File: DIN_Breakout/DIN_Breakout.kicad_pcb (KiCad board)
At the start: 2 copper layers, 33 x 23.2 mm, 2 parts, among them J1 Matra Alice, J2 Conn_01x08

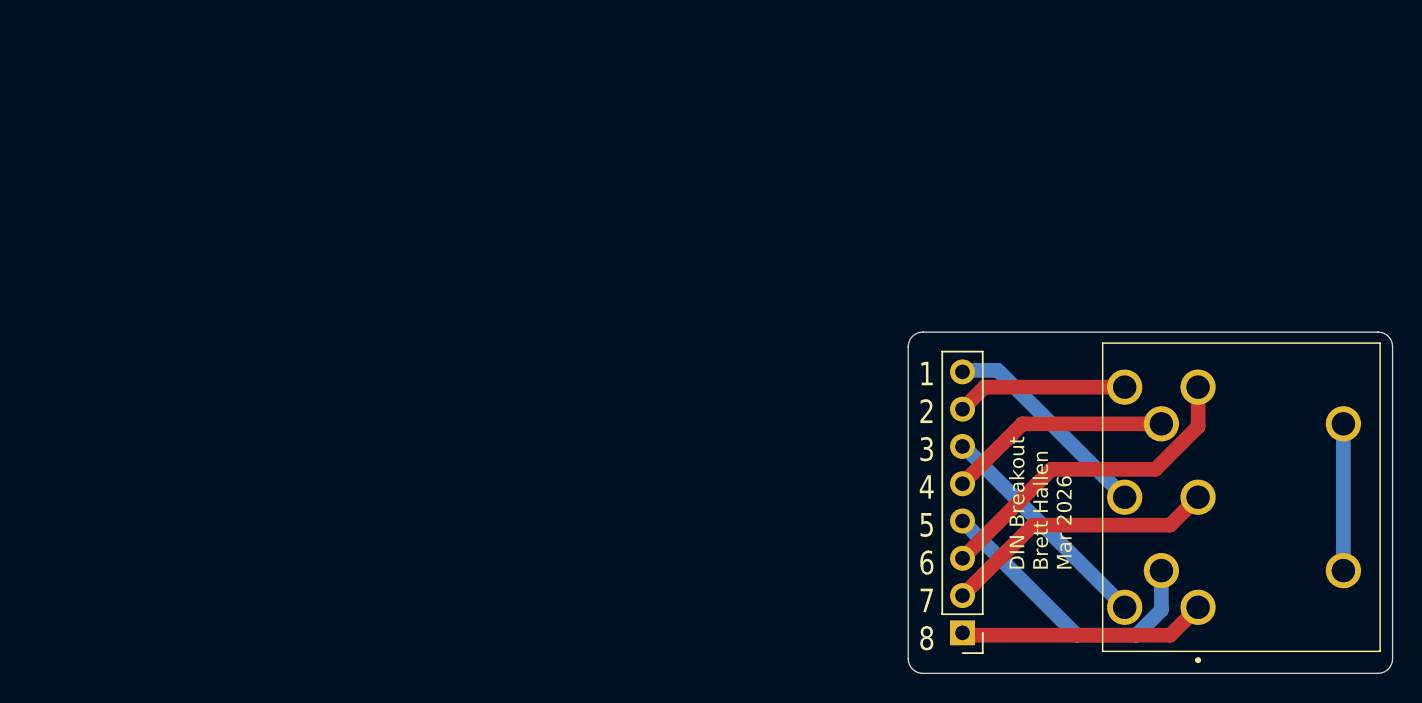
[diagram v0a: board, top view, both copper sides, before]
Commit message: Corrected silkscreen pin numbering
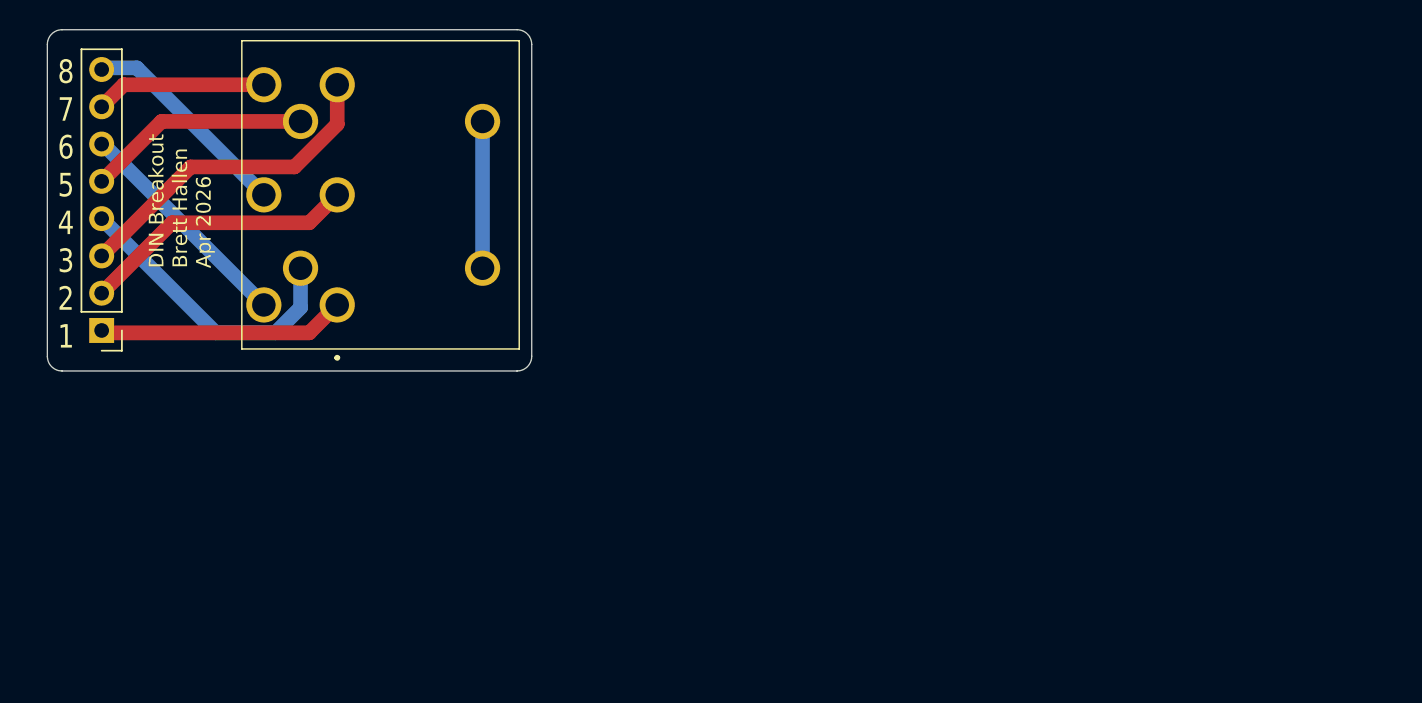
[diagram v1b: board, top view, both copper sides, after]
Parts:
- moved J1 62.2 mm to (93.4, 68.4)
- moved J2 62.2 mm to (77.3, 70.1)
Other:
- board text added: "DIN Breakout Brett Hallen Apr 2026"
- board text removed: "1 2 3 4 5 6 7 8"
- board text removed: "DIN Breakout Brett Hallen Mar 2026"
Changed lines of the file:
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@@
 		(legacy_teardrops no)
 	)
-	(paper "A4")
+	(paper "A5")
 	(title_block
 		(title "5/6/7/8 pin DIN Breakout Board")
-		(date "9/MAR/2026")
+		(date "29/APR/2026")
 		(rev "A")
 		(company "Brett Hallen")
@@
 	(footprint "Connector_PinHeader_2.54mm:PinHeader_1x08_P2.54mm_Vertical"
 		(layer "F.Cu")
-		(at 135.95 90.74 180)
+		(at 77.301 70.139 180)
 		(descr "Through hole straight pin header, 1x08, 2.54mm pitch, single row")
 		(tags "Through hole pin header THT 1x08 2.54mm single row")
@@
 	(footprint "Clueless_Engineer:6710801"
 		(layer "F.Cu")
-		(at 152 89 -90)
+		(at 93.351 68.399 -90)
 		(descr "DIN8")
 		(tags "Connector, DIN8")
@@
 	)
 	(gr_arc
-		(start 132.25 71.25)
-		(mid 132.542893 70.542893)
-		(end 133.25 70.25)
+		(start 73.601 50.649)
+		(mid 73.893893 49.941893)
+		(end 74.601 49.649)
 		(stroke
 			(width 0.05)
@@
 	)
 	(gr_line
-		(start 133.25 70.25)
-		(end 164.25 70.25)
+		(start 74.601 49.649)
+		(end 105.601 49.649)
 		(stroke
 			(width 0.05)
@@
 	)
 	(gr_arc
-		(start 164.25 70.25)
-		(mid 164.957107 70.542893)
-		(end 165.25 71.25)
+		(start 105.601 49.649)
+		(mid 106.308107 49.941893)
+		(end 106.601 50.649)
 		(stroke
 			(width 0.05)
@@
 	)
 	(gr_line
-		(start 165.25 71.25)
-		(end 165.25 92.5)
+		(start 106.601 50.649)
+		(end 106.601 71.899)
 		(stroke
 			(width 0.05)
@@
 	)
 	(gr_arc
-		(start 133.25 93.5)
-		(mid 132.542893 93.207107)
-		(end 132.25 92.5)
+		(start 74.601 72.899)
+		(mid 73.893893 72.606107)
+		(end 73.601 71.899)
 		(stroke
 			(width 0.05)
@@
 	)
 	(gr_line
-		(start 164.25 93.5)
-		(end 133.25 93.5)
+		(start 105.601 72.899)
+		(end 74.601 72.899)
 		(stroke
 			(width 0.05)
@@
 	)
 	(gr_line
-		(start 132.25 92.5)
-		(end 132.25 71.25)
+		(start 73.601 71.899)
+		(end 73.601 50.649)
 		(stroke
 			(width 0.05)
@@
 	)
 	(gr_arc
-		(start 165.25 92.5)
-		(mid 164.957107 93.207107)
-		(end 164.25 93.5)
+		(start 106.601 71.899)
+		(mid 106.308107 72.606107)
+		(end 105.601 72.899)
 		(stroke
 			(width 0.05)
@@
 		(layer "Edge.Cuts")
 	)
-	(gr_text "1\n2\n3\n4\n5\n6\n7\n8"
-		(at 132.95 92.1 0)
+	(gr_text "8\n7\n6\n5\n4\n3\n2\n1"
+		(at 74.301 71.499 0)
 		(layer "F.SilkS")
 		(effects
@@
 		)
 	)
-	(gr_text "DIN Breakout\nBrett Hallen\nMar 2026"
-		(at 143.5 86.5 90)
+	(gr_text "DIN Breakout\nBrett Hallen\nApr 2026"
+		(at 84.851 65.899 90)
 		(layer "F.SilkS")
 		(effects
@@
 	)
 	(gr_text "2"
-		(at 154.95 82.6 0)
+		(at 96.301 61.999 0)
 		(layer "B.SilkS")
 		(effects
@@
 	)
 	(gr_text "7"
-		(at 149.7 75.1 0)
+		(at 91.051 54.499 0)
 		(layer "B.SilkS")
 		(effects
@@
 	)
 	(gr_text "8\n7\n6\n5\n4\n3\n2\n1"
-		(at 134.45 92.1 0)
+		(at 75.801 71.499 0)
 		(layer "B.SilkS")
 		(effects
@@
 	)
 	(gr_text "3"
-		(at 154.95 75.1 0)
+		(at 96.301 54.499 0)
 		(layer "B.SilkS")
 		(effects
@@
 	)
 	(gr_text "4"
-		(at 152.45 87.5 0)
+		(at 93.801 66.899 0)
 		(layer "B.SilkS")
 		(effects
@@
 	)
 	(gr_text "6"
-		(at 149.7 90.1 0)
+		(at 91.051 69.499 0)
 		(layer "B.SilkS")
 		(effects
@@
 	)
 	(gr_text "1"
-		(at 154.7 90.1 0)
+		(at 96.051 69.499 0)
 		(layer "B.SilkS")
 		(effects
@@
 	)
 	(gr_text "5"
-		(at 152.7 77.6 0)
+		(at 94.051 56.999 0)
 		(layer "B.SilkS")
 		(effects
@@
 	)
 	(gr_text "8"
-		(at 149.7 82.6 0)
+		(at 91.051 61.999 0)
 		(layer "B.SilkS")
 		(effects
@@
 	)
 	(segment
-		(start 138.35 72.85)
-		(end 136.06 72.85)
+		(start 79.701 52.249)
+		(end 77.411 52.249)
 		(width 1)
 		(layer "B.Cu")
@@
 	)
 	(segment
-		(start 136.06 72.85)
-		(end 135.95 72.96)
+		(start 77.411 52.249)
+		(end 77.301 52.359)
 		(width 1)
 		(layer "B.Cu")
@@
 	)
 	(segment
-		(start 147 81.5)
-		(end 138.35 72.85)
+		(start 88.351 60.899)
+		(end 79.701 52.249)
 		(width 1)
 		(layer "B.Cu")
@@
 	)
 	(segment
-		(start 140.749 83.401)
-		(end 135.95 88.2)
+		(start 82.1 62.8)
+		(end 77.301 67.599)
 		(width 1)
 		(layer "F.Cu")
@@
 	)
 	(segment
-		(start 150.099 83.401)
-		(end 140.749 83.401)
+		(start 91.45 62.8)
+		(end 82.1 62.8)
 		(width 1)
 		(layer "F.Cu")
@@
 	)
 	(segment
-		(start 152 81.5)
-		(end 150.099 83.401)
+		(start 93.351 60.899)
+		(end 91.45 62.8)
 		(width 1)
 		(layer "F.Cu")
@@
 	)
 	(segment
-		(start 161.9 76.5)
-		(end 161.9 86.5)
+		(start 103.251 55.899)
+		(end 103.251 65.899)
 		(width 1)
 		(layer "B.Cu")
@@
 	)
 	(segment
-		(start 147 89)
-		(end 136.04 78.04)
+		(start 88.351 68.399)
+		(end 77.391 57.439)
 		(width 1)
 		(layer "B.Cu")
@@
 	)
 	(segment
-		(start 136.04 78.04)
-		(end 135.95 78.04)
+		(start 77.391 57.439)
+		(end 77.301 57.439)
 		(width 1)
 		(layer "B.Cu")
@@
 	)
 	(segment
-		(start 149.5 76.5)
-		(end 140.03 76.5)
+		(start 90.851 55.899)
+		(end 81.381 55.899)
 		(width 1)
 		(layer "F.Cu")
@@
 	)
 	(segment
-		(start 140.03 76.5)
-		(end 135.95 80.58)
+		(start 81.381 55.899)
+		(end 77.301 59.979)
 		(width 1)
 		(layer "F.Cu")
@@
 	)
 	(segment
-		(start 137.45 74)
-		(end 135.95 75.5)
+		(start 78.801 53.399)
+		(end 77.301 54.899)
 		(width 1)
 		(layer "F.Cu")
@@
 	)
 	(segment
-		(start 147 74)
-		(end 137.45 74)
+		(start 88.351 53.399)
+		(end 78.801 53.399)
 		(width 1)
 		(layer "F.Cu")
@@
 	)
 	(segment
-		(start 143.731 90.901)
-		(end 135.95 83.12)
+		(start 85.082 70.3)
+		(end 77.301 62.519)
 		(width 1)
 		(layer "B.Cu")
@@
 	)
 	(segment
-		(start 149.5 86.5)
-		(end 149.5 89.18842)
+		(start 90.851 65.899)
+		(end 90.851 68.58742)
 		(width 1)
 		(layer "B.Cu")
@@
 	)
 	(segment
-		(start 147.78742 90.901)
-		(end 143.731 90.901)
+		(start 89.13842 70.3)
+		(end 85.082 70.3)
 		(width 1)
 		(layer "B.Cu")
@@
 	)
 	(segment
-		(start 149.5 89.18842)
-		(end 147.78742 90.901)
+		(start 90.851 68.58742)
+		(end 89.13842 70.3)
 		(width 1)
 		(layer "B.Cu")
@@
 	)
 	(segment
-		(start 142.011 79.599)
-		(end 135.95 85.66)
+		(start 83.362 58.998)
+		(end 77.301 65.059)
 		(width 1)
 		(layer "F.Cu")
@@
 	)
 	(segment
-		(start 152 76.68842)
-		(end 149.08942 79.599)
+		(start 93.351 56.08742)
+		(end 90.44042 58.998)
 		(width 1)
 		(layer "F.Cu")
@@
 	)
 	(segment
-		(start 152 74)
-		(end 152 76.68842)
+		(start 93.351 53.399)
+		(end 93.351 56.08742)
 		(width 1)
 		(layer "F.Cu")
@@
 	)
 	(segment
-		(start 149.08942 79.599)
-		(end 142.011 79.599)
+		(start 90.44042 58.998)
+		(end 83.362 58.998)
 		(width 1)
 		(layer "F.Cu")
@@
 	)
 	(segment
-		(start 152 89)
-		(end 150.099 90.901)
+		(start 93.351 68.399)
+		(end 91.45 70.3)
 		(width 1)
 		(layer "F.Cu")
@@
 	)
 	(segment
-		(start 150.099 90.901)
-		(end 136.111 90.901)
+		(start 91.45 70.3)
+		(end 77.462 70.3)
 		(width 1)
 		(layer "F.Cu")
@@
 	)
 	(segment
-		(start 136.111 90.901)
-		(end 135.95 90.74)
+		(start 77.462 70.3)
+		(end 77.301 70.139)
 		(width 1)
 		(layer "F.Cu")
@@
 	)
 	(segment
-		(start 136.111 90.901)
-		(end 135.95 90.74)
+		(start 77.462 70.3)
+		(end 77.301 70.139)
 		(width 1)
 		(layer "B.Cu")

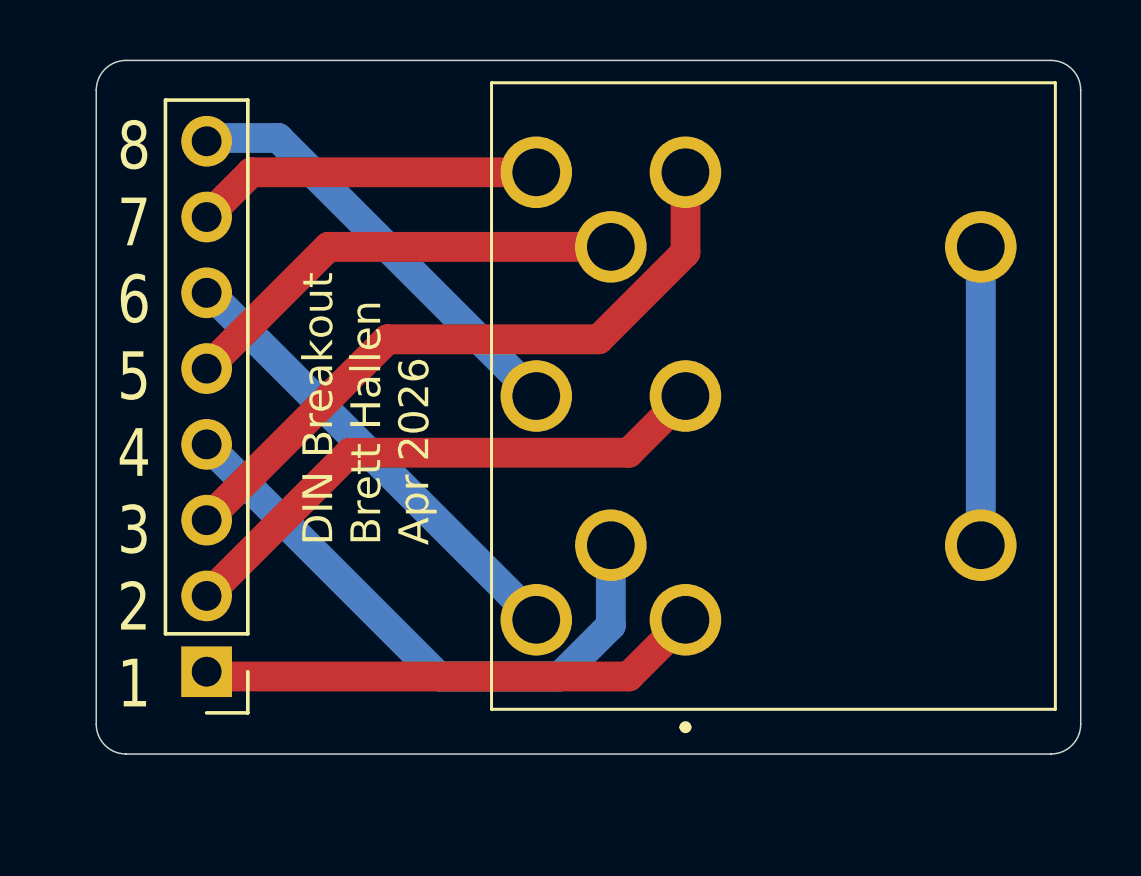
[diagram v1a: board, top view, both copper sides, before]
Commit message: Added breakout pin for shield
Sometimes ground is only on shield
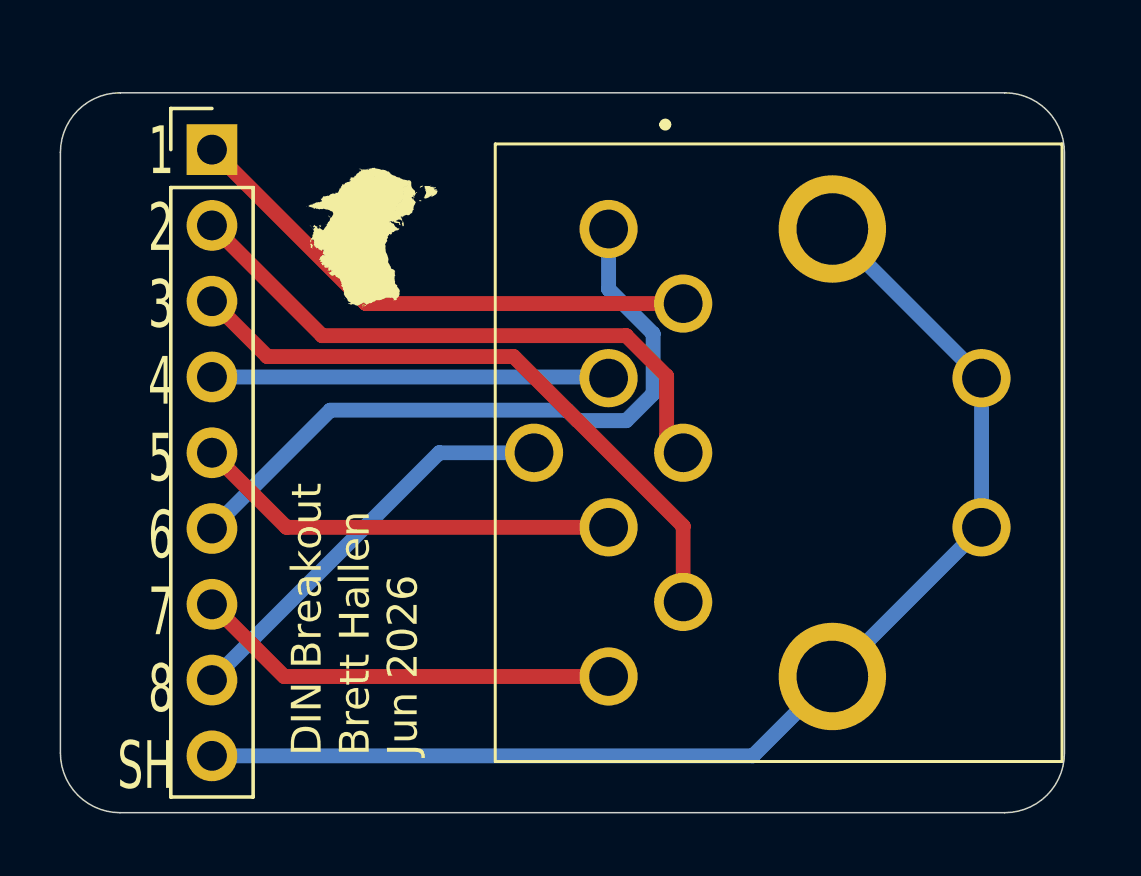
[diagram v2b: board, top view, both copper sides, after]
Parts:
- J1: value Matra Alice -> DIN Socket; footprint Clueless_Engineer:6710801 -> Clueless_Engineer:SDF80J
- J2: value Conn_01x08 -> Breakout; footprint Connector_PinHeader_2.54mm:PinHeader_1x08_P2.54mm_Vertical -> Connector_PinHeader_2.54mm:PinHeader_1x09_P2.54mm_Vertical
- moved J2 17.5 mm to (77.5, 52.6), turned to 0 degrees
- moved J1 10.6 mm to (93.3, 57.8), turned to 90 degrees
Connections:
- net Net-(J2-Pin_1) renamed /Pin 1
- net Net-(J2-Pin_2) renamed /Pin 2
- net Net-(J2-Pin_3) renamed /Pin 3
- net Net-(J2-Pin_4) renamed /Pin 4
- net Net-(J2-Pin_5) renamed /Pin 5
- net Net-(J2-Pin_6) renamed /Pin 6
- net Net-(J2-Pin_7) renamed /Pin 7
- net Net-(J2-Pin_8) renamed /Pin 8
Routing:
- net /Shield: track 0.00 -> 41.0 mm
- net GND: track 10.0 -> 0.00 mm
- net /Pin 6: track 15.6 -> 23.1 mm
- net /Pin 4: track 20.2 -> 13.3 mm
- net /Pin 7: track 11.7 -> 14.3 mm
- net /Pin 2: track 18.8 -> 20.1 mm
- net /Pin 3: track 22.5 -> 21.5 mm
- net /Pin 5: track 15.2 -> 14.3 mm
- net /Pin 1: track 17.1 -> 17.9 mm
- net /Pin 8: track 14.7 -> 14.0 mm
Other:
- board size 33 x 23.2 mm -> 33.7 x 24.1 mm
- board text added: "1 2 3 4 5 6 7 8 SH"
- board text added: "DIN Breakout Brett Hallen Jun 2026"
- board text removed: "8 7 6 5 4 3 2 1"
- board text removed: "DIN Breakout Brett Hallen Apr 2026"
